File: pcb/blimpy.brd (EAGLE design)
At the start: 85 x 55 mm, 42 parts, among them IC1 TB6612FNG, J2 MICRO-USB, J3 JSTPH, Q1 mmbt2222, Q2 mmbt2222, Q3 DMG3415U, U1 RGB, U2 AP2112-3.3, U3 MCP73831T-2, U4 BNO080, U7 CP2104, U9 ESP-WROOM-32

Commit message: updated board design
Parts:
- removed C11: 10uF, SparkFun-Capacitors:0603
- removed IC1: TB6612FNG, adafruit:SSOP24
- added C12, C14, C15, C16, C17, C18, C19, C21, C22, C24, C25, C27: 0.1uF, SparkFun-Capacitors:0603
- added C28, C29, C30, C31: 10uF, SparkFun-Capacitors:EIA3216
- added C9: 10uF, SparkFun-Capacitors:0603
- added CN1, CN2, CN3, CN4, CN5, CN6, CN7, CN8: (no value), adafruit:JST-PH-2-SMT-RA
- added HB1, HB2, HB3, HB4: TB6612FNG, adafruit:SSOP24
- added J1: JSTPH, microbuilder:JSTPH2
- added U5, U6: SX1509, SparkFun-IC-Special-Function:QFN-28
- R4: value 4.7k -> 2.0k
- moved R13 180.5 mm to (231.7, 82.6)
- moved U9 179.9 mm to (226.4, 102.8)
- moved R11 179.5 mm to (231.8, 114.7)
- moved R14 178.7 mm to (233.5, 82.5)
- moved R5 178.7 mm to (227.8, 82.6)
- moved R6 178.7 mm to (225.9, 82.6)
- moved R7 178.7 mm to (224.1, 82.6)
- moved U1 178.7 mm to (218.1, 82.6)
- moved C13 132.9 mm to (33.8, 142.5), turned to 90 degrees
- moved C5 128.2 mm to (33.8, 138.5), turned to 270 degrees
- moved R1 76.2 mm to (42.3, 101.3)
- moved R3 76.2 mm to (42.3, 98.9)
- moved R8 74.8 mm to (57.9, 74.7)
- moved R15 70.6 mm to (57.4, 71.8)
- moved C1 66.7 mm to (47.9, 75.6)
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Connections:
- removed net N$20: IC1.5, IC1.6
- removed net N$24: IC1.11, IC1.12
- removed net VBAT: C11.1, C3.1, C5.1, IC1.13, IC1.14, IC1.24, J3.2, Q3.3, R1.2, U3.3
- removed net VBUS: D1.A, D2.A, J2.VBUS, Q3.1, R12.2, U3.4, U7.8
- new net IO1_RST: U5.23
- new net IO2_RST: U6.23
- new net M1_DIR: U5.19, U6.19
- new net M1_PWM: U5.20, U6.20
- new net M2_DIR: U5.21, U6.21
- new net M2_PWM: U5.22, U6.22
- new net M3_DIR: U5.13, U6.13
- new net M3_PWM: U5.14, U6.14
- new net M4_DIR: U5.15, U6.15
- new net M4_PWM: U5.16, U6.16
- new net M5_DIR: U5.5, U6.5
- new net M5_PWM: U5.6, U6.6
- new net M6_DIR: U5.7, U6.7
- new net M6_PWM: U5.8, U6.8
- new net N$17: CN1.2, HB1.5, HB1.6
- new net N$21: CN2.2, HB1.11, HB1.12
- new net N$23: CN3.1, HB2.1, HB2.2
- new net N$25: CN3.2, HB2.5, HB2.6
- new net N$33: CN4.2, HB2.11, HB2.12
- new net N$35: CN5.2, HB3.5, HB3.6
- new net N$37: CN6.2, HB3.11, HB3.12
- new net N$38: CN7.1, HB4.1, HB4.2
- new net N$39: CN7.2, HB4.5, HB4.6
- new net N$41: CN8.2, HB4.11, HB4.12
- new net N$5: CN1.1, HB1.1, HB1.2
- new net S1_SIG: U5.27, U6.27
- new net S2_SIG: U5.28, U6.28
- new net S3_SIG: U5.1, U6.1
- new net S4_SIG: U5.2, U6.2
- new net V_BATT: C19.1, C22.1, C25.1, C28.+, C29.+, C3.1, C30.+, C31.+, C5.1, HB1.13, HB1.14, HB1.24, HB2.13, HB2.14, HB2.24, HB3.13, HB3.14, HB3.24, HB4.13, HB4.14, HB4.24, J3.2, Q3.3, R1.2, U3.3
- new net V_USB: C9.1, D1.A, D2.A, J2.VBUS, Q3.1, R12.2, U3.4, U7.8
- net 3.3V: now also C12.1, C14.1, C15.1, C16.1, C17.1, C18.1, C21.1, C24.1, C27.1, HB1.19, HB1.20, HB2.19, HB2.20, HB3.19, HB3.20, HB4.19, HB4.20, U5.12, U5.18, U5.4, U6.12, U6.18, U6.26, U6.4; no longer IC1.19, IC1.20
- net GND: now also C12.2, C14.2, C15.2, C16.2, C17.2, C18.2, C19.2, C21.2, C22.2, C24.2, C25.2, C27.2, C28.-, C29.-, C30.-, C31.-, C9.2, HB1.10, HB1.18, HB1.3, HB1.4, HB1.9, HB2.10, HB2.18, HB2.3, HB2.4, HB2.9, HB3.10, HB3.18, HB3.3, HB3.4, HB3.9, HB4.10, HB4.18, HB4.3, HB4.4, HB4.9, U5.10, U5.17, U5.26, U5.29, U5.3, U6.10, U6.17, U6.29, U6.3; no longer C11.2, IC1.10, IC1.18, IC1.3, IC1.4, IC1.9
- net N$18: now also CN5.1, HB3.1, HB3.2; no longer IC1.1, IC1.2
- net N$22: now also CN2.1, CN4.1, CN6.1, CN8.1, HB1.7, HB1.8, HB2.7, HB2.8, HB3.7, HB3.8, HB4.7, HB4.8; no longer IC1.7, IC1.8
- net N$26: now also HB1.15, HB2.15, HB3.15, HB4.15; no longer IC1.15
- net N$27: now also HB1.16, HB2.16, HB3.16, HB4.16; no longer IC1.16
- net N$28: now also HB1.17, HB2.17, HB3.17, HB4.17; no longer IC1.17
- net N$30: now also HB1.21, HB2.21, HB3.21, HB4.21; no longer IC1.21
- net N$31: now also HB1.22, HB2.22, HB3.22, HB4.22; no longer IC1.22
- net N$32: now also HB1.23, HB2.23, HB3.23, HB4.23; no longer IC1.23
- net SCL: now also U5.25, U6.25
- net SDA: now also U5.24, U6.24
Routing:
- removed copper zone on layer 16, net 3.3V
- removed copper zone on layer 1, net GND
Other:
- board size 85 x 55 mm -> 250 x 167 mm
- board text removed: "+"
- board text removed: "-"

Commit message: updated
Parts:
- removed CN1, CN2, CN3, CN4, CN5, CN6, CN7, CN8: (no value), adafruit:JST-PH-2-SMT-RA
- removed J3: JSTPH, microbuilder:JSTPH2
- added J10, J11, J12, J13, J14, J15, J8, J9: (no value), SparkFun-Connectors:JST-2-SMD
- added J4, J5, J6, J7: 3-PIN SMD, SparkFun-Connectors:JST-3-SMD
- added JP1: JUMPER-SMT_2_NO_SILK, SparkFun-Jumpers:SMT-JUMPER_2_NO_SILK
- J1: value JSTPH -> MICRO-USB; device microbuilder:JSTPH2 -> SparkFun-Connectors:USB-MICROB
- J2: value MICRO-USB -> (none); device SparkFun-Connectors:USB-MICROB -> SparkFun-Connectors:JST-2-SMD
- moved C25 95.0 mm to (77.6, 24.6)
- moved C31 95.0 mm to (90.0, 25.0)
- moved HB4 95.0 mm to (92.4, 15.2)
- moved C27 95.0 mm to (94.2, 24.6)
- moved C16 70.0 mm to (60.6, 12.2)
- moved C17 70.0 mm to (63.9, 12.2)
- moved C18 70.0 mm to (60.6, 8.90)
- moved U6 70.0 mm to (62.0, 18.2)
- moved C22 54.0 mm to (30.3, 9.60)
- moved C24 54.0 mm to (36.2, 7.70)
- moved C30 54.0 mm to (24.0, 9.00)
- moved HB3 54.0 mm to (28.2, 19.2)
- moved J1 28.1 mm to (5.80, 90.2), turned to 180 degrees
- moved J2 10.8 mm to (6.00, 101.0), turned to 90 degrees
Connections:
- removed net M1_DIR: U5.19, U6.19
- removed net M1_PWM: U5.20, U6.20
- removed net M2_DIR: U5.21, U6.21
- removed net M2_PWM: U5.22, U6.22
- removed net M3_DIR: U5.13, U6.13
- removed net M3_PWM: U5.14, U6.14
- removed net M4_DIR: U5.15, U6.15
- removed net M4_PWM: U5.16, U6.16
- removed net M5_DIR: U5.5, U6.5
- removed net M5_PWM: U5.6, U6.6
- removed net M6_DIR: U5.7, U6.7
- removed net M6_PWM: U5.8, U6.8
- removed net N$26: HB1.15, HB2.15, HB3.15, HB4.15
- removed net N$27: HB1.16, HB2.16, HB3.16, HB4.16
- removed net N$28: HB1.17, HB2.17, HB3.17, HB4.17
- removed net N$30: HB1.21, HB2.21, HB3.21, HB4.21
- removed net N$31: HB1.22, HB2.22, HB3.22, HB4.22
- removed net N$32: HB1.23, HB2.23, HB3.23, HB4.23
- removed net S1_SIG: U5.27, U6.27
- removed net S2_SIG: U5.28, U6.28
- removed net S3_SIG: U5.1, U6.1
- removed net S4_SIG: U5.2, U6.2
- new net 1-1: U5.27
- new net 1-10: U5.14
- new net 1-11: U5.15
- new net 1-12: U5.16
- new net 1-13: U5.19
- new net 1-14: U5.20
- new net 1-15: U5.21
- new net 1-16: U5.22
- new net 1-2: U5.28
- new net 1-3: U5.1
- new net 1-4: U5.2
- new net 1-5: U5.5
- new net 1-6: U5.6
- new net 1-7: U5.7
- new net 1-8: U5.8
- new net 1-9: U5.13
- new net 2-1: U6.27
- new net 2-10: U6.14
- new net 2-11: U6.15
- new net 2-12: U6.16
- new net 2-13: U6.19
- new net 2-14: U6.20
- new net 2-15: U6.21
- new net 2-16: U6.22
- new net 2-2: U6.28
- new net 2-3: U6.1
- new net 2-4: U6.2
- new net 2-5: U6.5
- new net 2-6: U6.6
- new net 2-7: U6.7
- new net 2-8: U6.8
- new net 2-9: U6.13
- new net H1-1: HB1.23
- new net H1-2: HB1.22
- new net H1-3: HB1.21
- new net H1-4: HB1.17
- new net H1-5: HB1.16
- new net H1-6: HB1.15
- new net H2-1: HB2.23
- new net H2-2: HB2.22
- new net H2-3: HB2.21
- new net H2-4: HB2.17
- new net H2-5: HB2.16
- new net H2-6: HB2.15
- new net H3-1: HB3.23
- new net H3-2: HB3.22
- new net H3-3: HB3.21
- new net H3-4: HB3.17
- new net H3-5: HB3.16
- new net H3-6: HB3.15
- new net H4-1: HB4.23
- new net H4-2: HB4.22
- new net H4-3: HB4.21
- new net H4-4: HB4.17
- new net H4-5: HB4.16
- new net H4-6: HB4.15
- new net N$19: J4.3, J5.3, J6.3, J7.3
- net GND: now also J1.GND, J1.MT1, J1.MT2, J1.P$1, J1.P$2, J2.1, J4.2, J5.2, J6.2, J7.2; no longer J2.GND, J2.MT1, J2.MT2, J2.P$1, J2.P$2, J3.1
- net N$17: now also J8.2; no longer CN1.2
- net N$18: now also J12.1; no longer CN5.1
- net N$2: now also J1.D+; no longer J2.D+
- net N$21: now also J9.2; no longer CN2.2
- net N$22: now also J11.1, J13.1, J15.1, J9.1; no longer CN2.1, CN4.1, CN6.1, CN8.1
- net N$23: now also J10.1; no longer CN3.1
- net N$25: now also J10.2; no longer CN3.2
- net N$33: now also J11.2; no longer CN4.2
- net N$35: now also J12.2; no longer CN5.2
- net N$37: now also J13.2; no longer CN6.2
- net N$38: now also J14.1; no longer CN7.1
- net N$39: now also J14.2; no longer CN7.2
- net N$4: now also JP1.1
- net N$41: now also J15.2; no longer CN8.2
- net N$5: now also J8.1; no longer CN1.1
- net N$6: now also J1.D-; no longer J2.D-
- net V_BATT: now also J2.2, J4.1, J5.1, J6.1, J7.1; no longer J3.2
- net V_USB: now also J1.VBUS, JP1.2; no longer J2.VBUS

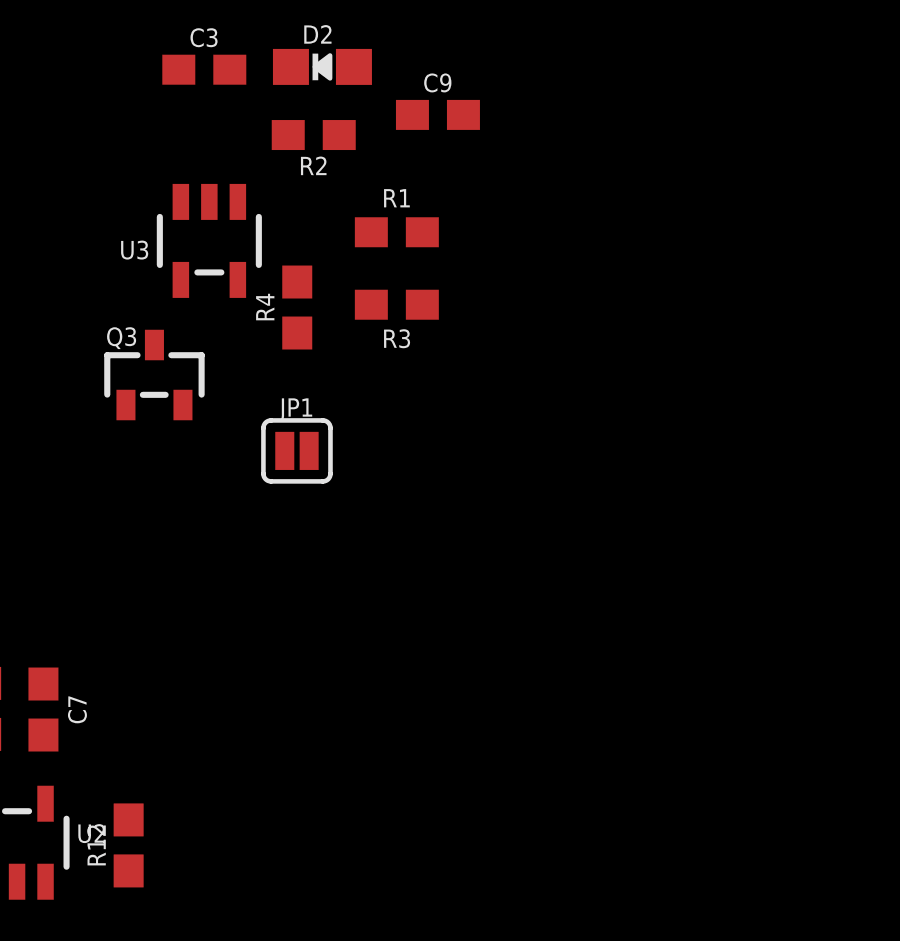
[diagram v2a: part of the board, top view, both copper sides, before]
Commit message: added battery gauge
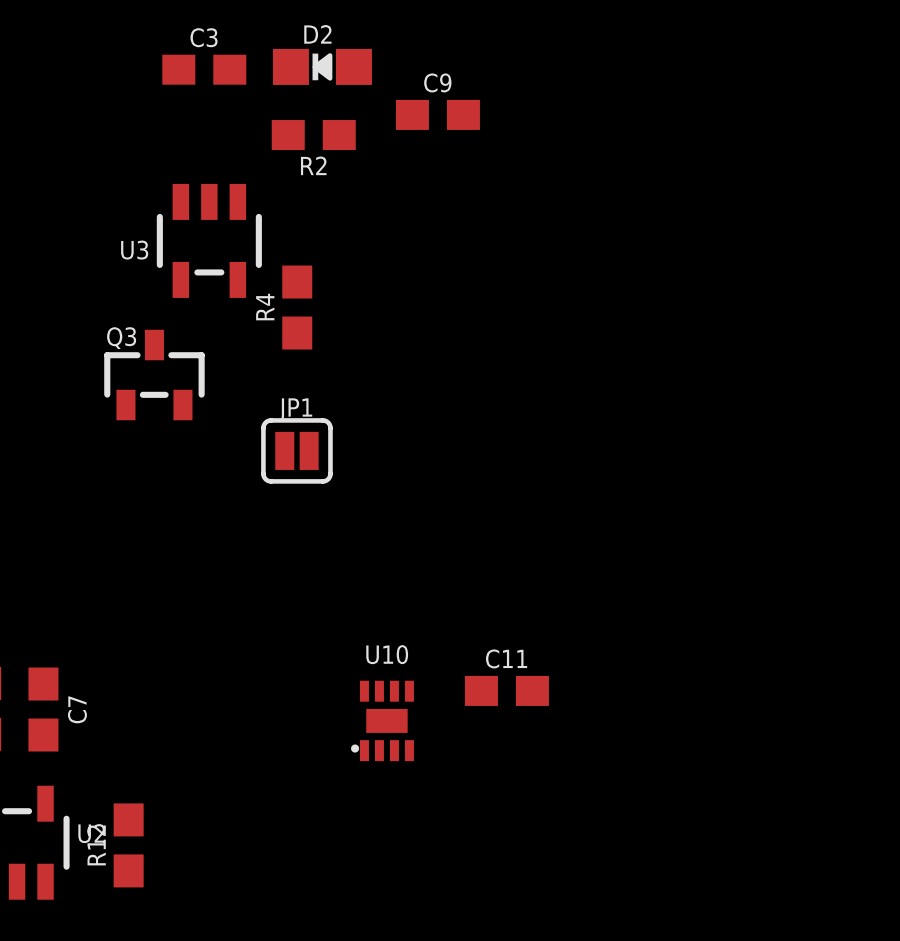
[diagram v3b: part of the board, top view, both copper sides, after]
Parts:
- removed R1, R3: 100k, SparkFun-Resistors:0603
- added C11: 0.1uF, SparkFun-Capacitors:0603
- added U10: MAX17048, SparkFun-IC-Power:DFN-8
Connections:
- removed net BAT: R1.1, R3.2, U9.6
- net GND: now also C11.2, U10.P$1, U10.P$4, U10.P$6, U10.P$9; no longer R3.1
- net SCL: now also U10.P$7
- net SDA: now also U10.P$8
- net V_BATT: now also C11.1, U10.P$2, U10.P$3; no longer R1.2

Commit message: updated
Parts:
- moved C24 17.1 mm to (21.7, 16.8), turned to 270 degrees
- moved C27 14.6 mm to (85.6, 12.8), turned to 270 degrees
- moved J14 14.4 mm to (89.2, 3.20)
- moved J12 14.4 mm to (24.2, 6.60)
- moved C22 13.6 mm to (22.3, 20.6)
- moved C31 12.2 mm to (83.0, 15.0), turned to 270 degrees
- moved J13 12.2 mm to (33.2, 6.90)
- moved J15 11.7 mm to (98.2, 3.50)
- moved C25 11.2 mm to (86.4, 17.6), turned to 90 degrees
- moved C30 11.2 mm to (19.0, 19.0), turned to 270 degrees
- moved C19 9.84 mm to (94.8, 138.4), turned to 270 degrees
- moved C21 9.23 mm to (95.2, 143.2), turned to 90 degrees
- moved J5 4.00 mm to (128.0, 154.0)
- moved C29 2.24 mm to (99.0, 141.0), turned to 90 degrees
- moved C28 1.84 mm to (38.0, 140.0)
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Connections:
- removed net N$17: HB1.5, HB1.6, J8.2
- removed net N$18: HB3.1, HB3.2, J12.1
- removed net N$21: HB1.11, HB1.12, J9.2
- removed net N$22: HB1.7, HB1.8, HB2.7, HB2.8, HB3.7, HB3.8, HB4.7, HB4.8, J11.1, J13.1, J15.1, J9.1
- removed net N$23: HB2.1, HB2.2, J10.1
- removed net N$25: HB2.5, HB2.6, J10.2
- removed net N$33: HB2.11, HB2.12, J11.2
- removed net N$35: HB3.5, HB3.6, J12.2
- removed net N$37: HB3.11, HB3.12, J13.2
- removed net N$38: HB4.1, HB4.2, J14.1
- removed net N$39: HB4.5, HB4.6, J14.2
- removed net N$41: HB4.11, HB4.12, J15.2
- removed net N$5: HB1.1, HB1.2, J8.1
- new net HB1-A1: HB1.1, HB1.2, J8.2
- new net HB1-A2: HB1.5, HB1.6, J8.1
- new net HB1-B1: HB1.11, HB1.12, J9.1
- new net HB1-B2: HB1.7, HB1.8, J9.2
- new net HB2-A1: HB2.1, HB2.2, J10.2
- new net HB2-A2: HB2.5, HB2.6, J10.1
- new net HB2-B1: HB2.11, HB2.12, J11.1
- new net HB2-B2: HB2.7, HB2.8, J11.2
- new net HB3-A1: HB3.1, HB3.2, J12.2
- new net HB3-A2: HB3.5, HB3.6, J12.1
- new net HB3-B1: HB3.11, HB3.12, J13.1
- new net HB3-B2: HB3.7, HB3.8, J13.2
- new net HB4-A1: HB4.1, HB4.2, J14.2
- new net HB4-A2: HB4.5, HB4.6, J14.1
- new net HB4-B1: HB4.11, HB4.12, J15.1
- new net HB4-B2: HB4.7, HB4.8, J15.2

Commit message: updated
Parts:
- moved J12 164.0 mm to (88.5, 157.5), turned to 0 degrees
- moved J13 157.3 mm to (78.5, 157.5), turned to 0 degrees
- moved J14 155.6 mm to (109.5, 157.5), turned to 0 degrees
- moved J15 154.0 mm to (99.5, 157.5), turned to 0 degrees
- moved J6 147.3 mm to (147.0, 158.5), turned to 0 degrees
- moved J7 147.3 mm to (159.0, 158.5), turned to 0 degrees
- moved C30 143.3 mm to (90.0, 143.5)
- moved C24 137.6 mm to (75.5, 143.5), turned to 90 degrees
- moved HB3 136.0 mm to (83.5, 143.5), turned to 180 degrees
- moved C22 134.7 mm to (77.5, 143.5)
- moved C31 131.5 mm to (111.0, 143.5)
- moved C27 131.2 mm to (96.5, 143.5), turned to 90 degrees
- moved HB4 128.9 mm to (104.5, 143.5), turned to 180 degrees
- moved C25 126.5 mm to (98.5, 143.5)
- moved C18 122.2 mm to (95.5, 126.0), turned to 270 degrees
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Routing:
- net V_BATT: track 0.00 -> 77.9 mm
- net HB4-A2: track 0.00 -> 11.2 mm
- net HB3-B2: track 0.00 -> 11.2 mm
- net HB2-A2: track 0.00 -> 11.2 mm
- net HB1-B2: track 0.00 -> 11.2 mm
- net HB4-B2: track 0.00 -> 11.2 mm
- net HB3-A2: track 0.00 -> 11.2 mm
- net HB2-B2: track 0.00 -> 11.2 mm
- net HB1-A2: track 0.00 -> 11.2 mm
- net HB4-B1: track 0.00 -> 9.92 mm
- net HB4-A1: track 0.00 -> 9.92 mm
- net HB3-B1: track 0.00 -> 9.92 mm
- net HB3-A1: track 0.00 -> 9.92 mm
- net HB2-A1: track 0.00 -> 9.92 mm
- net HB2-B1: track 0.00 -> 9.92 mm
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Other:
- board text added: "Trace Widths for 1oz Copper: Logic: 0.4mm, 15mil Actors: 0.8mm, 30mil (2A) Battery: 1.6mm, 60mil (4A) Text Sizes Vector, 0.6, 15%"

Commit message: updated
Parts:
- moved C3 4.30 mm to (42.0, 49.5)
- moved C2 3.35 mm to (18.5, 33.0)
- moved JP1 2.24 mm to (46.0, 41.5)
- moved R4 2.24 mm to (45.5, 45.5)
- moved Q3 2.06 mm to (42.0, 41.5)
- moved C1 1.58 mm to (53.5, 19.5)
- moved C11 1.58 mm to (51.5, 29.5)
- moved C4 1.12 mm to (53.5, 17.0)
- moved R16 1.12 mm to (62.5, 15.0)
- moved R15 0.71 mm to (62.5, 17.5)
- moved C10 0.50 mm to (53.5, 15.0)
- moved C6 0.50 mm to (33.0, 22.5)
- moved R8 0.50 mm to (62.5, 20.0)
- turned U5 to 180 degrees
- turned U6 to 180 degrees
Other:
- board text added: "M1"
- board text added: "M2"
- board text added: "M3"
- board text added: "M4"
- board text added: "M5"
- board text added: "M6"
- board text added: "M7"
- board text added: "M8"
- board text added: "S1"
- board text added: "S2"
- board text added: "S3"
- board text added: "S4"

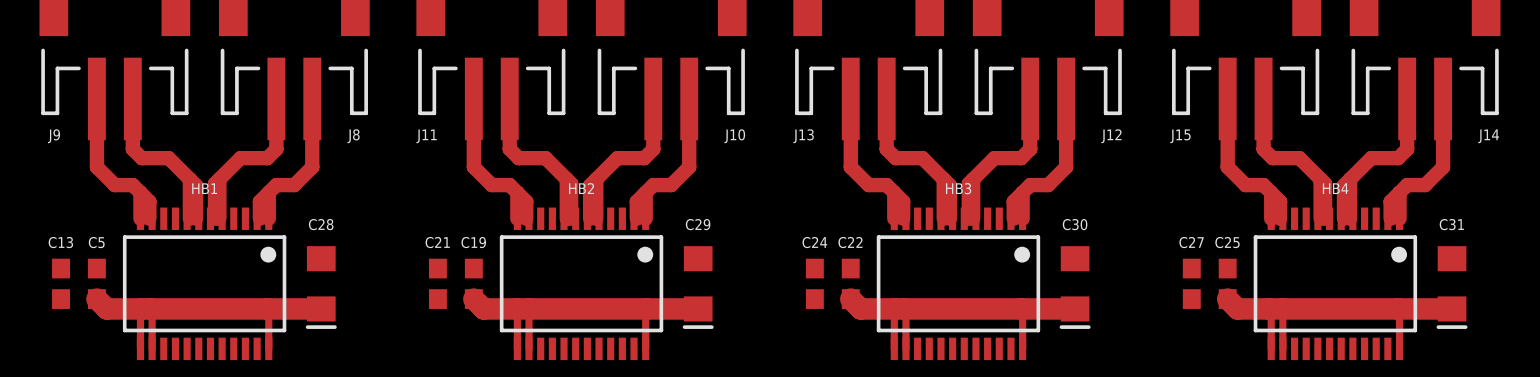
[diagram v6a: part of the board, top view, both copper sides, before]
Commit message: improved hbridge traces
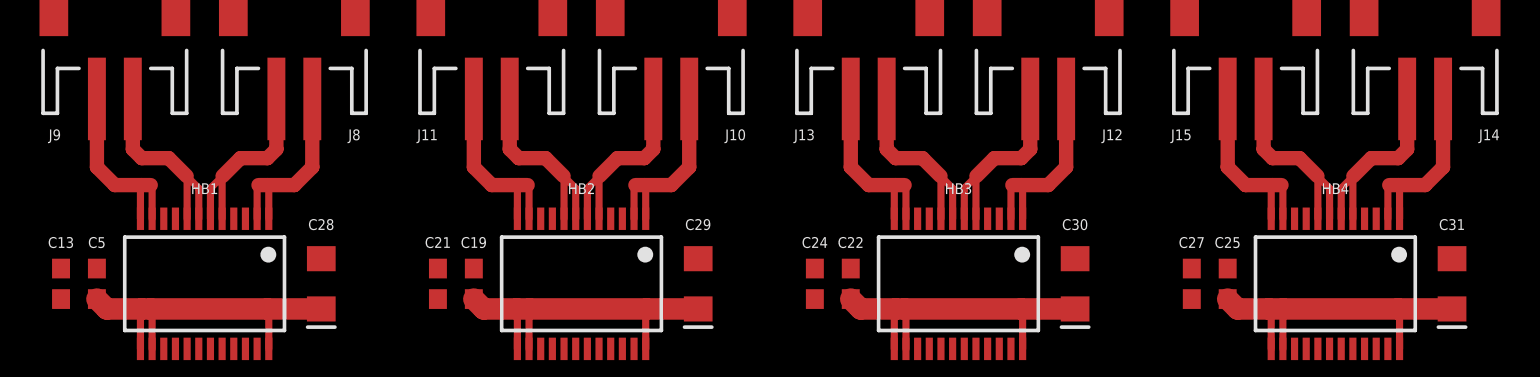
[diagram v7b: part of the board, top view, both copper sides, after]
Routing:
- net HB2-B1: track 9.92 -> 11.0 mm
- net HB1-B1: track 9.92 -> 11.0 mm
- net HB1-A1: track 9.92 -> 11.0 mm
- net HB4-B1: track 9.92 -> 11.0 mm
- net HB4-A1: track 9.92 -> 11.0 mm
- net HB3-B1: track 9.92 -> 11.0 mm
- net HB3-A1: track 9.92 -> 11.0 mm
- net HB2-A1: track 9.92 -> 11.0 mm
